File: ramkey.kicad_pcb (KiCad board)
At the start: 2 copper layers, 99.7 x 94.3 mm, 4 parts, among them SW1 SW_Push

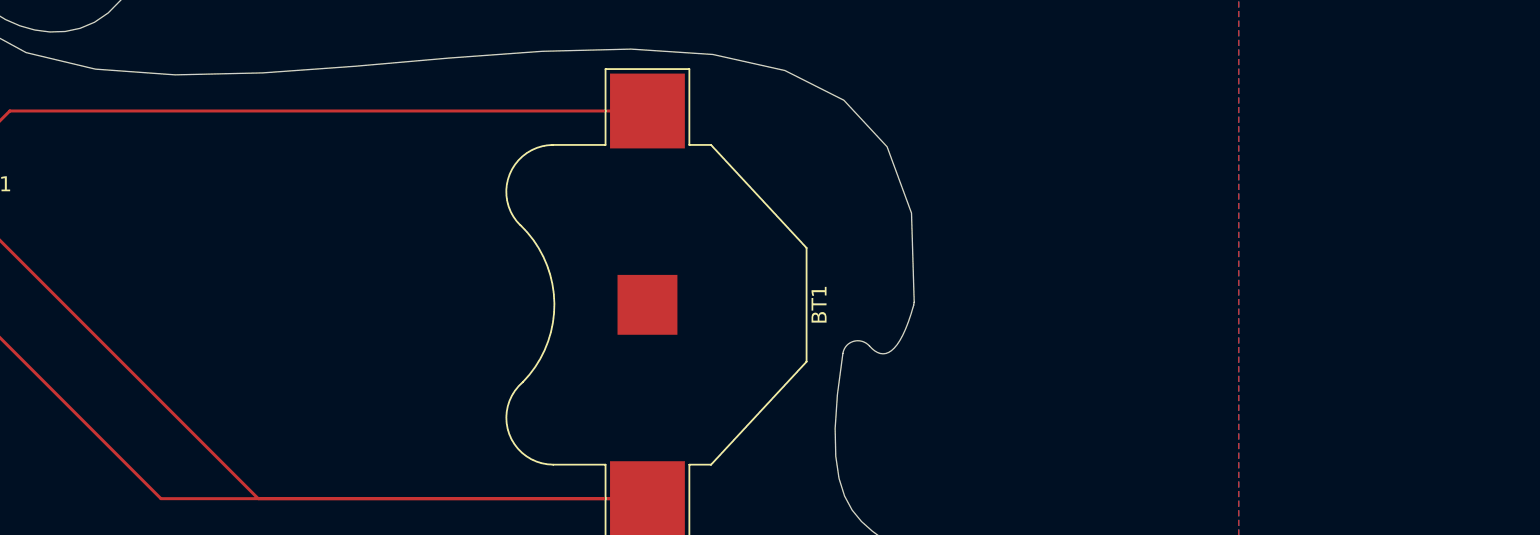
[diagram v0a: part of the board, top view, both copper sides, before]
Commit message: feat: add silkscreen
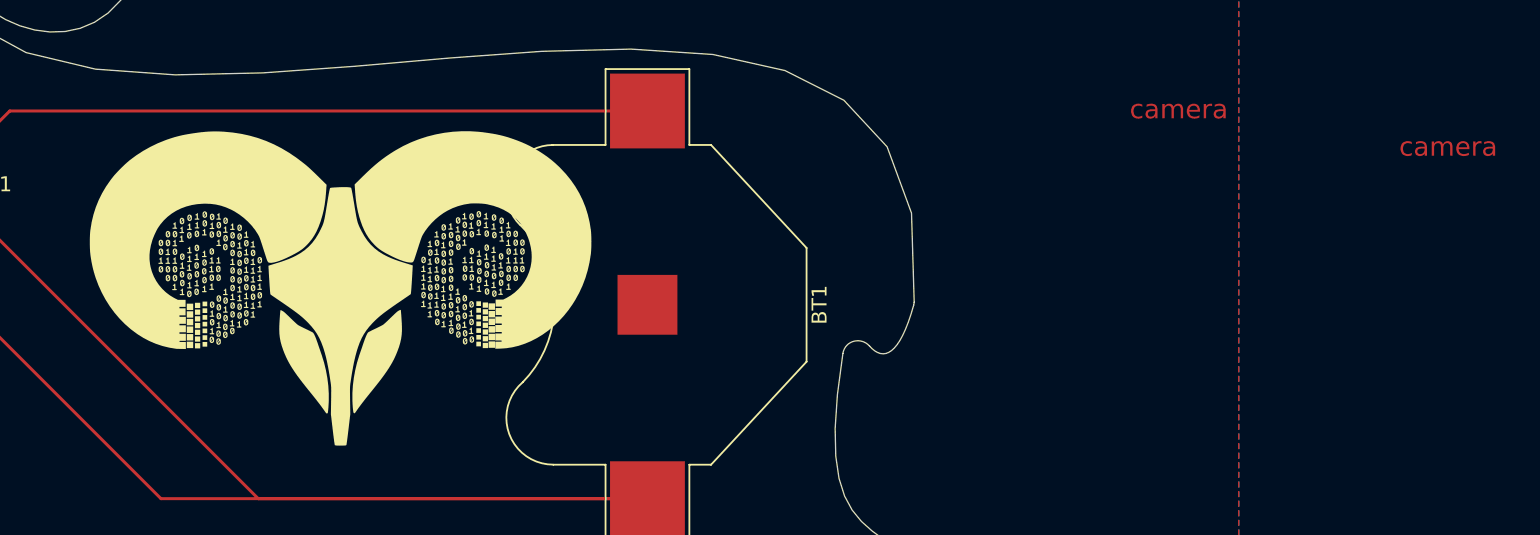
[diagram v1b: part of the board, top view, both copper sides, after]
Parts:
- added G***: LOGO, LOGO, F.Cu at (160.5, 98.0)
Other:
- board text added: "camera"
